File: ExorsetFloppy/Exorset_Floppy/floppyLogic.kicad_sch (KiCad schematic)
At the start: 76 parts, among them J10 Conn_01x01, J11 Conn_01x01, J12 Conn_01x01, J13 Conn_01x01, J14 Conn_01x01, J15 Conn_01x01, J16 Conn_01x01, J17 Conn_01x01, J18 Conn_01x01, J19 Conn_01x01, J2 Floppy, J20 Conn_01x01, J21 Conn_01x01, J22 Conn_01x01, J3 Conn_01x01, J7 Conn_01x17, J8 Conn_01x01, J9 Conn_01x01, Q1 BC337, U10 GAL16V8, U11 74HCT74, U12 74HCT74, U13 74LS91, U15 74HCT04, U16 74HCT74, U17 74HCT00, U18 74HCT74, U19 74LS76, U2 74HCT74, U20 68B21, U21 MC4024, U22 74LS157, U23 74LS123, U24 74HCT164, U25 74LS04, U27 MC4044, U28 74F163, U29 74F163, U34 6852_DIL24, U4 MC8506, U5 74F163, U7 74HCT240, U8 74HCT244, U9 NE7555P

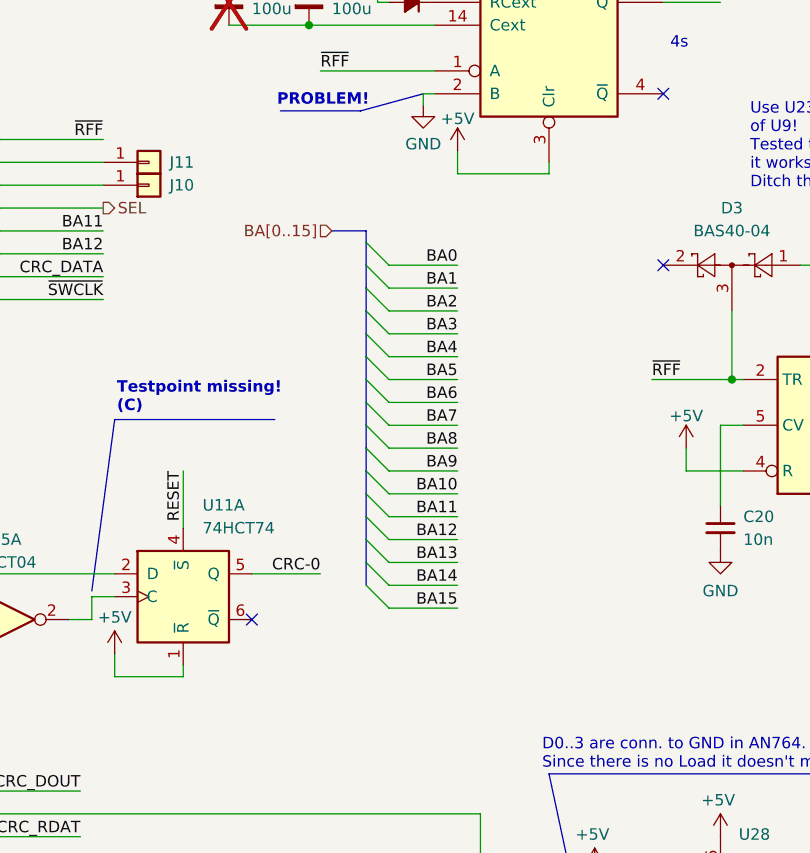
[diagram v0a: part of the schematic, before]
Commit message: new GAL eq. for additional EPROM on board
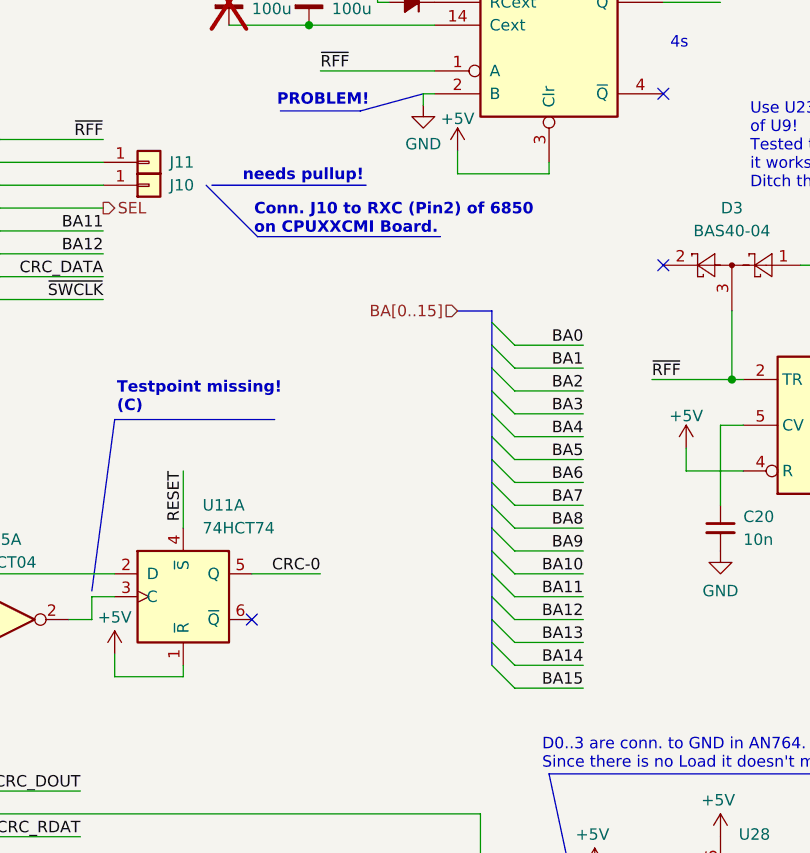
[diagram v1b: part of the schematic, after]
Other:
- note added: "Conn. J10 to RXC (Pin2) of 6850 on CPUXXCMI Board."
- note added: "needs pullup!"

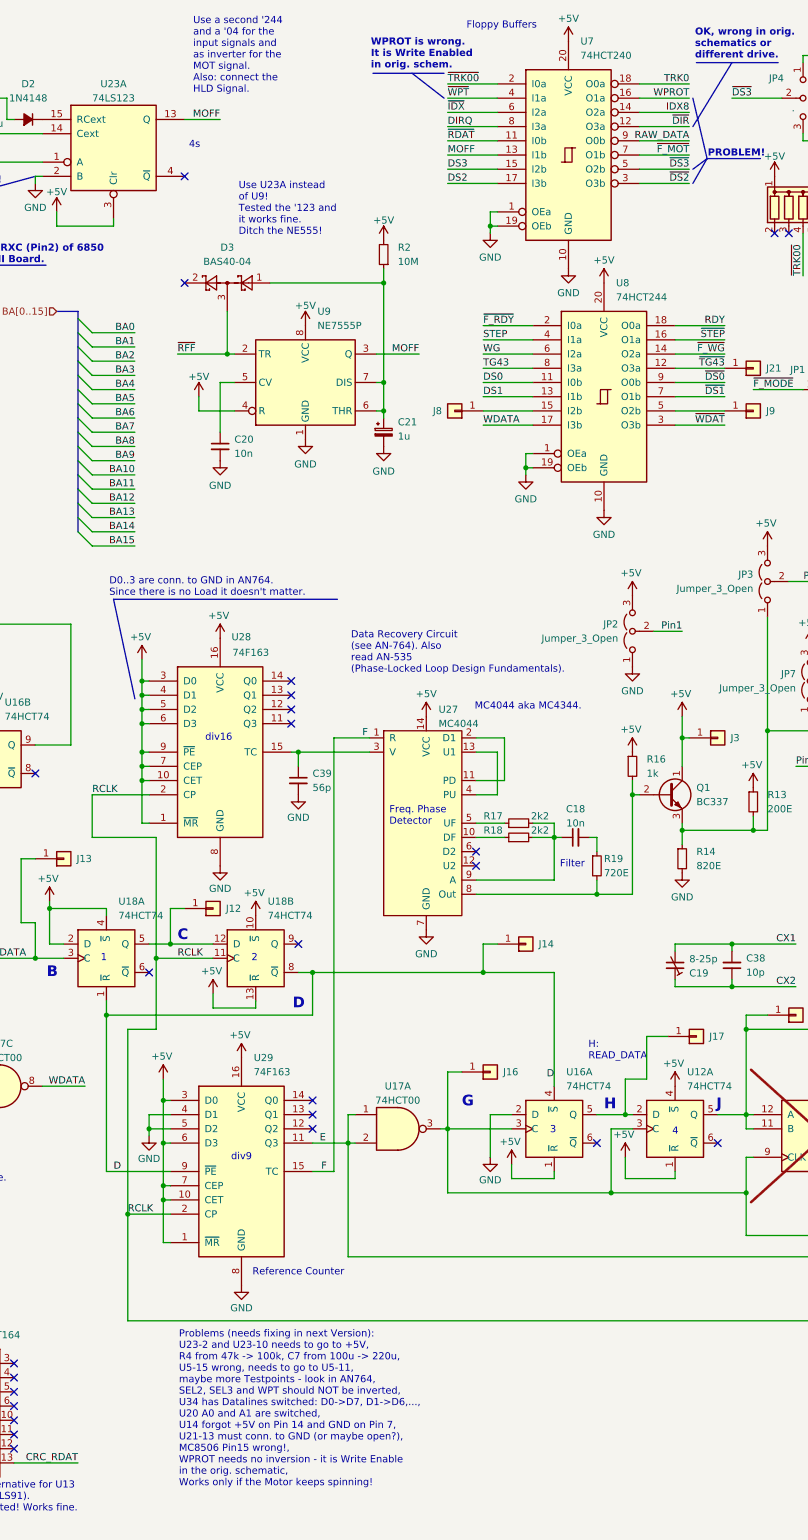
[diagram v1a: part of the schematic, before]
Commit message: new build for extra drives
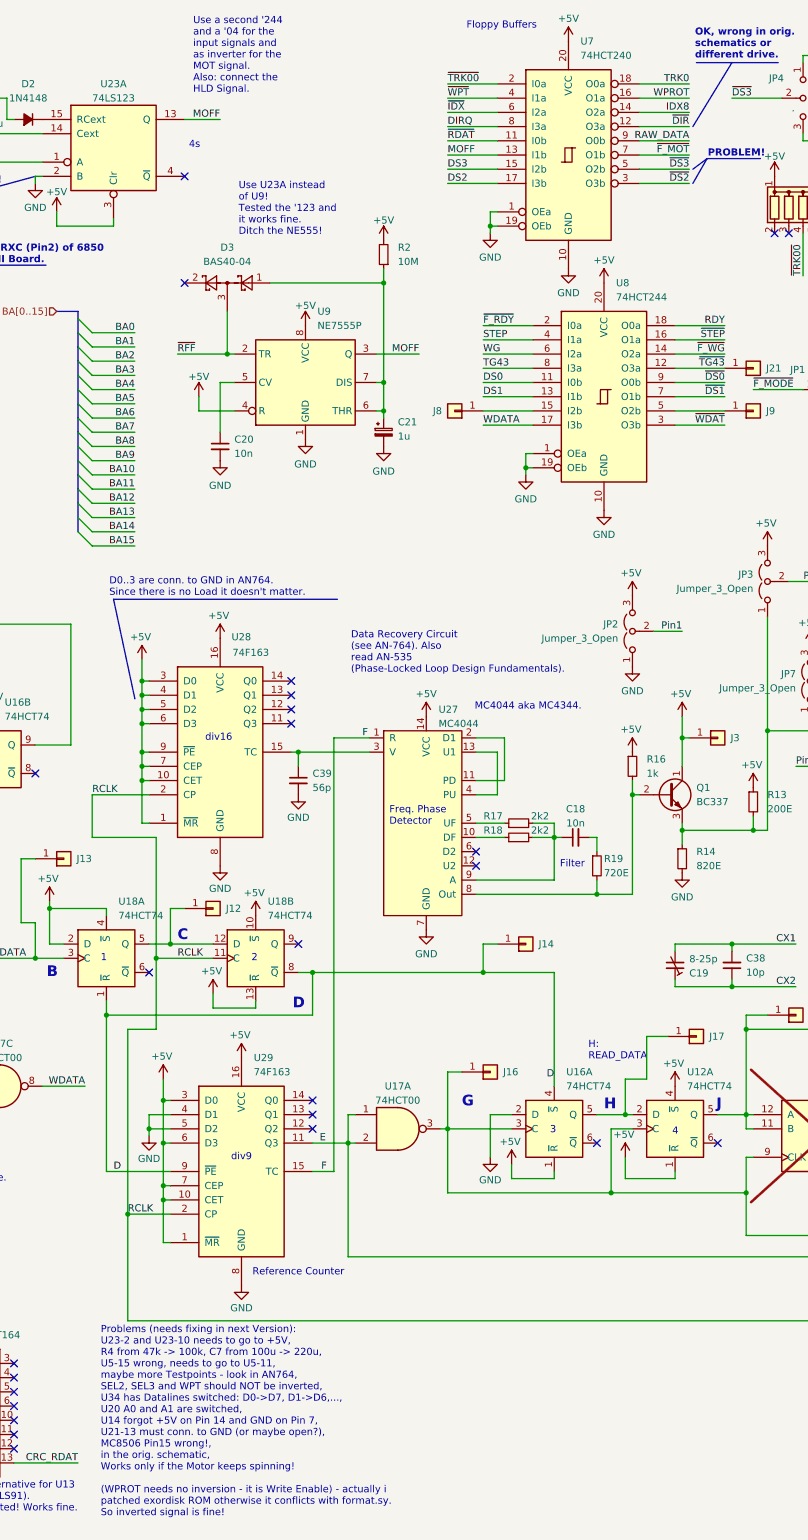
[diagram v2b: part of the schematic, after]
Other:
- note removed: "WPROT is wrong. It is Write Enabled in orig. schem."
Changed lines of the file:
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@@
 		)
 	)
-	(text "WPROT is wrong.\nIt is Write Enabled\nin orig. schem."
-		(exclude_from_sim no)
-		(at 278.384 20.066 0)
-		(effects
-			(font
-				(size 1.27 1.27)
-				(thickness 0.254)
-				(bold yes)
-			)
-			(justify left)
-		)
-	)
 	(text "PROBLEM!"
 		(exclude_from_sim no)
@@
 		)
 	)
-	(text "Problems (needs fixing in next Version):\nU23-2 and U23-10 needs to go to +5V,\nR4 from 47k -> 100k, C7 from 100u -> 220u,\nU5-15 wrong, needs to go to U5-11,\nmaybe more Testpoints - look in AN764,\nSEL2, SEL3 and WPT should NOT be inverted,\nU34 has Datalines switched: D0->D7, D1->D6,...,\nU20 A0 and A1 are switched,\nU14 forgot +5V on Pin 14 and GND on Pin 7,\nU21-13 must conn. to GND (or maybe open?),\nMC8506 Pin15 wrong!,\nWPROT needs no inversion - it is Write Enable\nin the orig. schematic,\nWorks only if the Motor keeps spinning!"
+	(text "Problems (needs fixing in next Version):\nU23-2 and U23-10 needs to go to +5V,\nR4 from 47k -> 100k, C7 from 100u -> 220u,\nU5-15 wrong, needs to go to U5-11,\nmaybe more Testpoints - look in AN764,\nSEL2, SEL3 and WPT should NOT be inverted,\nU34 has Datalines switched: D0->D7, D1->D6,...,\nU20 A0 and A1 are switched,\nU14 forgot +5V on Pin 14 and GND on Pin 7,\nU21-13 must conn. to GND (or maybe open?),\nMC8506 Pin15 wrong!,\nin the orig. schematic,\nWorks only if the Motor keeps spinning!\n\n(WPROT needs no inversion - it is Write Enable) - actually i \npatched exordisk ROM otherwise it conflicts with format.sy. \nSo inverted signal is fine!"
 		(exclude_from_sim no)
-		(at 244.094 262.128 0)
+		(at 230.124 264.414 0)
 		(effects
 			(font
@@
 		)
 	)
-	(polyline
-		(pts
-			(xy 285.75 23.495) (xy 291.465 27.94)
-		)
-		(stroke
-			(width 0)
-			(type default)
-		)
-	)
 	(wire
 		(pts
@@
 		)
 	)
-	(polyline
-		(pts
-			(xy 335.915 27.94) (xy 338.455 38.735)
-		)
-		(stroke
-			(width 0)
-			(type default)
-		)
-	)
 	(wire
 		(pts
@@
 		)
 		(stroke
-			(width 0)
-			(type default)
-		)
-	)
-	(polyline
-		(pts
-			(xy 278.765 23.495) (xy 291.465 23.495)
-		)
-		(stroke
